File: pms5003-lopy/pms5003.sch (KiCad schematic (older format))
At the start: 11 parts, among them J1 Battery, J2 DS3231, J3 PMS5003, J4 SHT10, J5 P2, J6 PROG, Q1 IRF540N, U1 U3V12F5, U11 LoPy4

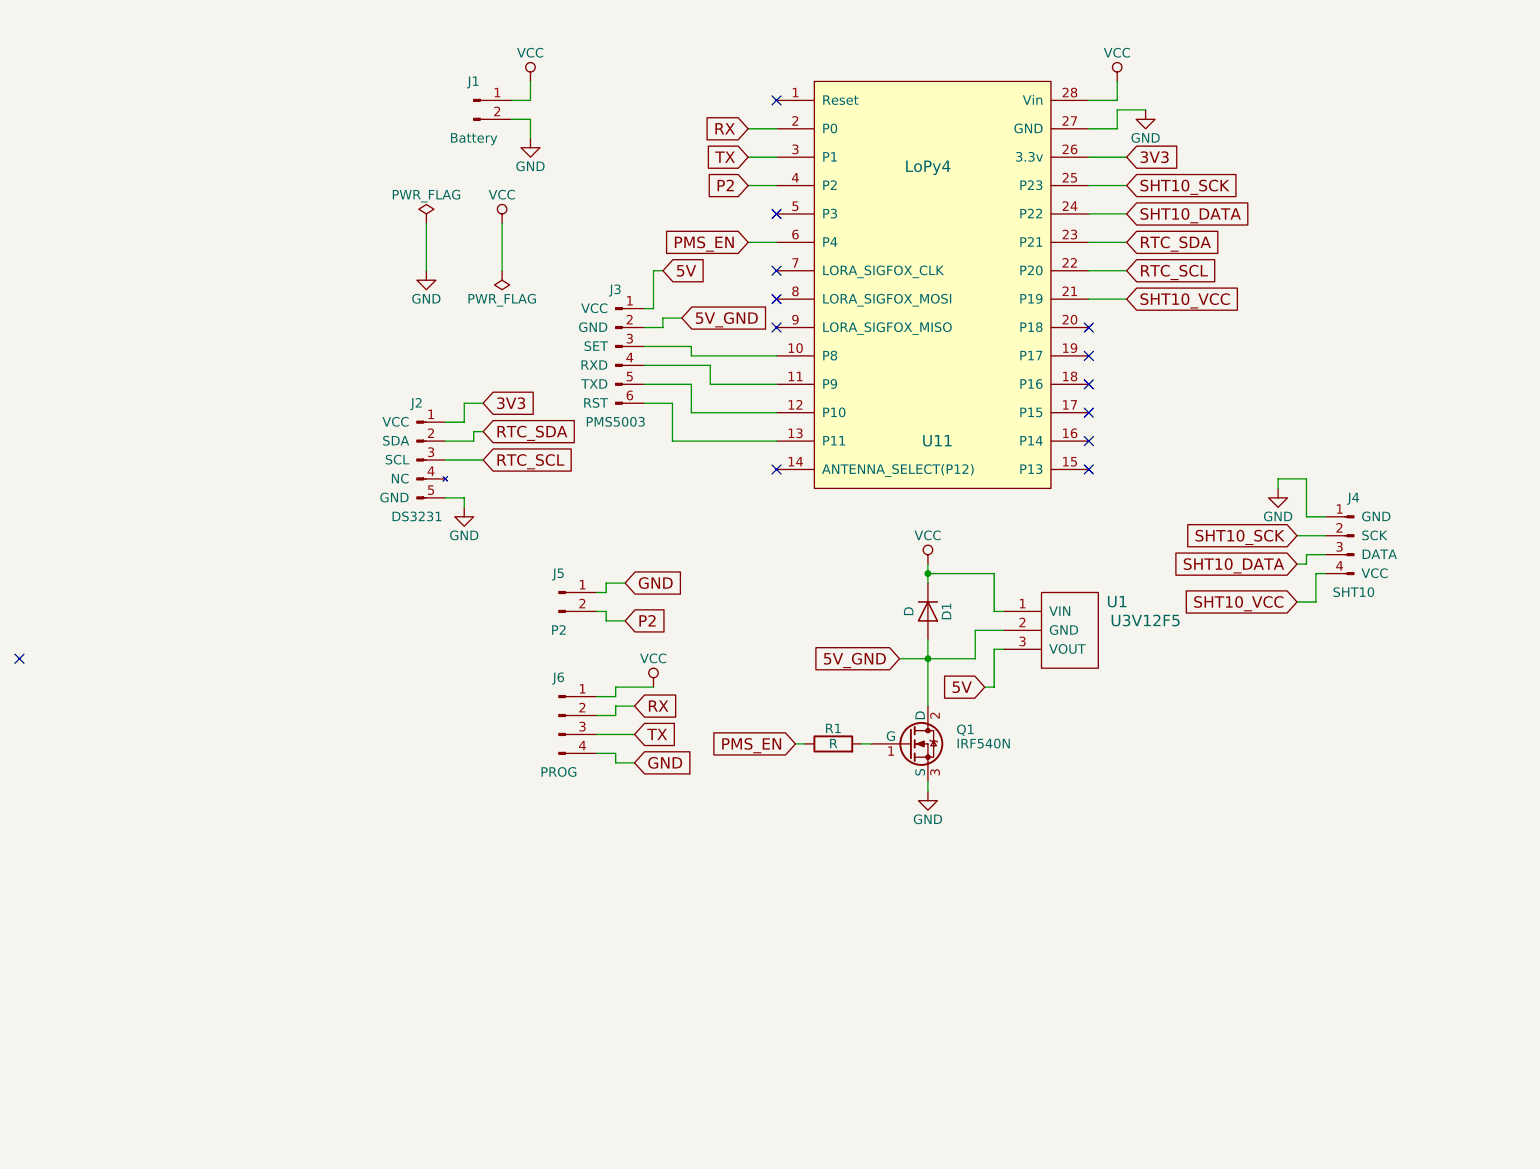
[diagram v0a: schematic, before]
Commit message: PMS5003: Add battery charger circuit
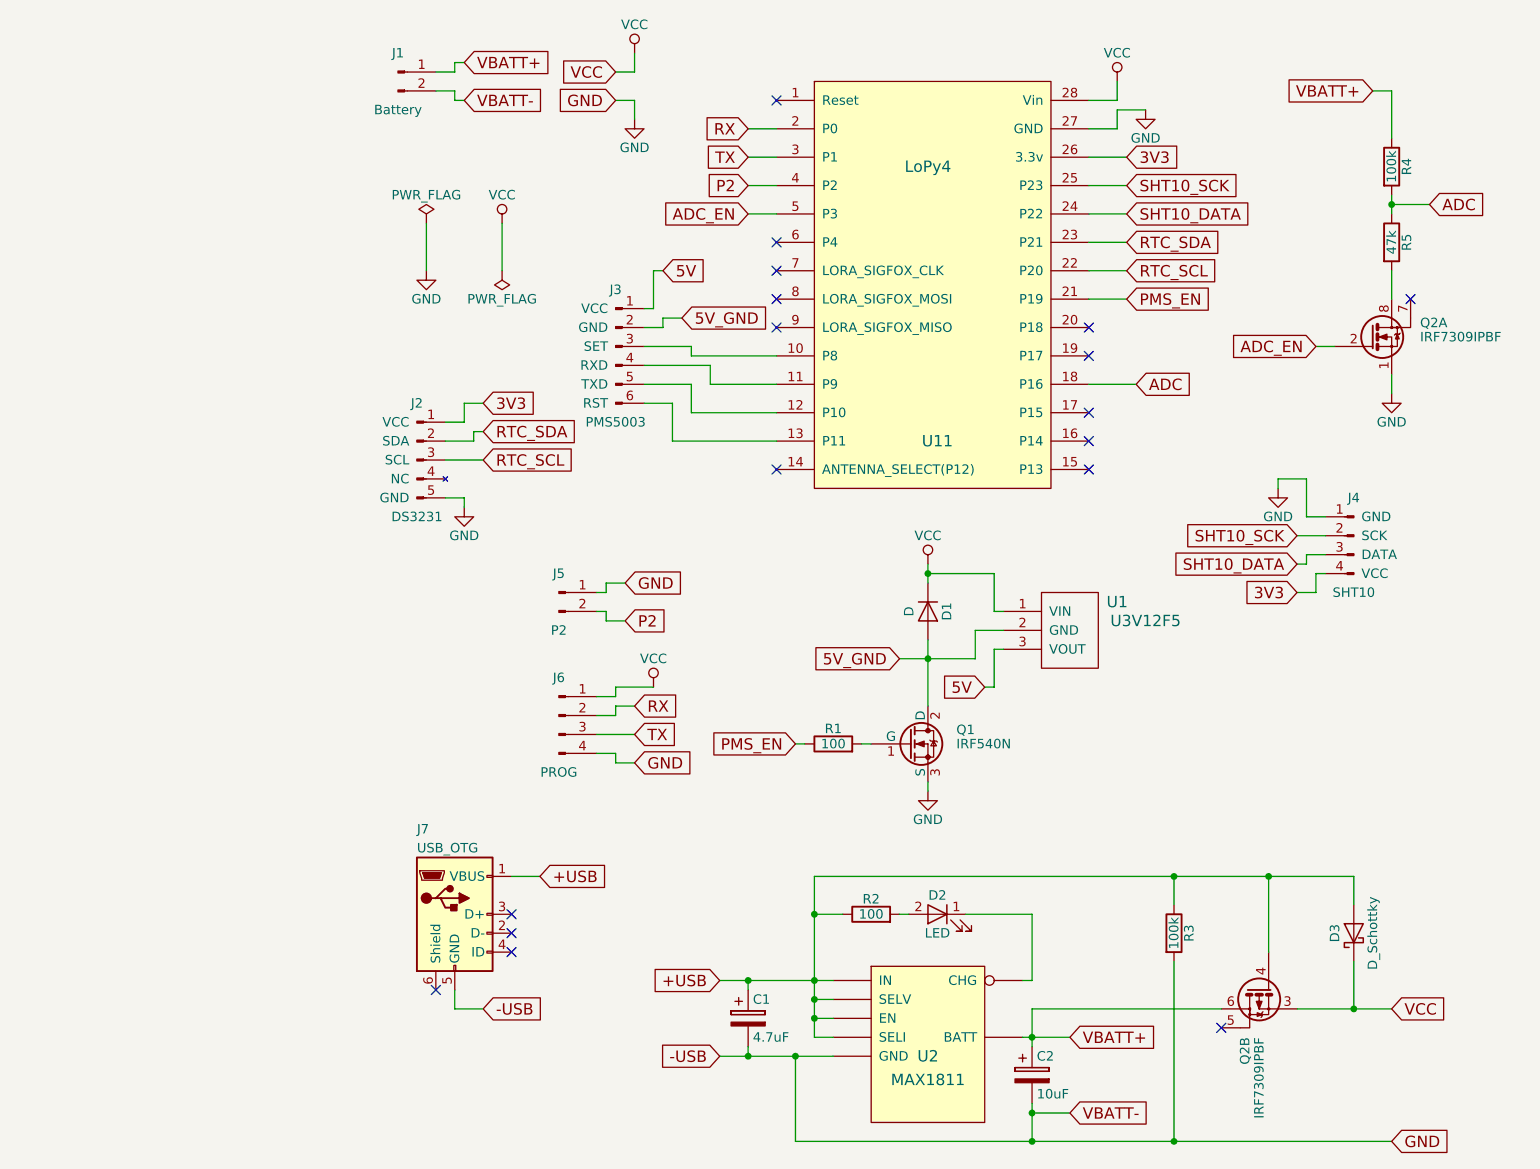
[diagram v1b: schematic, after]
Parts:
- added C1: 4.7uF, Capacitors_Tantalum_SMD:CP_Tantalum_Case-A_EIA-3216-18_Reflow, symbol CP
- added C2: 10uF, Capacitors_Tantalum_SMD:CP_Tantalum_Case-A_EIA-3216-18_Reflow, symbol CP
- added D2: LED, LEDs:LED_1206, symbol LED
- added D3: D_Schottky, Diodes_SMD:D_SMA, symbol D_Schottky
- added J7: USB_OTG, Connectors:USB_Micro-B, symbol USB_OTG
- added Q2: IRF7309IPBF, Housings_SOIC:SO-8_5.3x6.2mm_Pitch1.27mm, symbol IRF7309IPBF
- added R2: 100, Resistors_SMD:R_1206, symbol R
- added R3, R4: 100k, Resistors_SMD:R_1206, symbol R
- added R5: 47k, Resistors_SMD:R_1206, symbol R
- added U2: MAX1811, Power_Integrations:SO-8, symbol MAX1811
- R1: value R -> 100
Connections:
- net 3V3: now also J4.4 (VCC)
- net GND: now also C1.2, C2.2, J7.5 (GND), Q2.1 (S), R3.2, U2.3 (GND)
- net PMS_EN: now also U11.21 (P19); no longer U11.6 (P4)
- net VCC: now also D3.1 (K), Q2.3 (1); no longer J1.1 (Pin_1)
- net ADC: now reaches U11.18 (P16)
- net ADC: now also R4.2, R5.1
- net ADC_EN: now reaches U11.5 (P3)
- net ADC_EN: now also Q2.2 (G)
- removed net SHT10_VCC: J4.4 (VCC), U11.21 (P19)
- new net: Q2.8 (D), R5.2
- new net: D2.1 (K), U2.8 (CHG)
- new net: D2.2 (A), R2.2
- new net +USB: C1.1, D3.2 (A), J7.1 (VBUS), Q2.4 (G), R2.1, R3.1, U2.1 (SELV), U2.2 (SELI), U2.4 (IN), U2.7 (EN)
- new net VBATT+: C2.1, J1.1 (Pin_1), Q2.6 (D), R4.1, U2.5 (BATT)
- no-connect marks 13 -> 17
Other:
- moved on the sheet: J1
